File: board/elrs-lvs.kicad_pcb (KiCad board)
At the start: 4 copper layers, 46 x 22 mm, 85 parts, among them J1 PWM, J10 CF/Prog, J12 Balance, J13 U.FL, J2 PWM, J3 PWM, J4 PWM, J5 PWM, J6 PWM, J7 PWM, J8 PWM, J9 Little Tower, SW1 SW_SPST, SW2 SW_SPST, U1 ESP32-PICO-V3, U2 SX1281, U3 TPSM82901SISR, U4 2450FM07D0034T, Y1 52Mhz TCXO

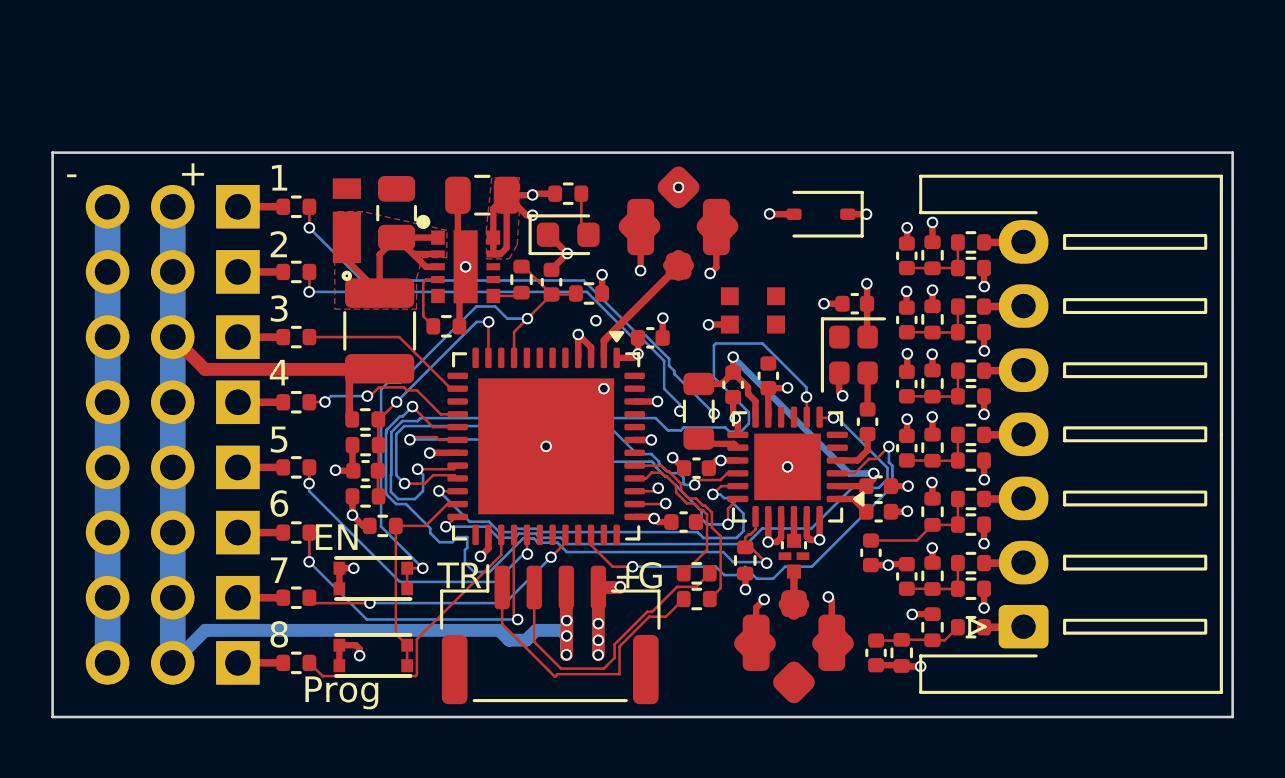
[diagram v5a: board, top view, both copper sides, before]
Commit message: rotate and initial route
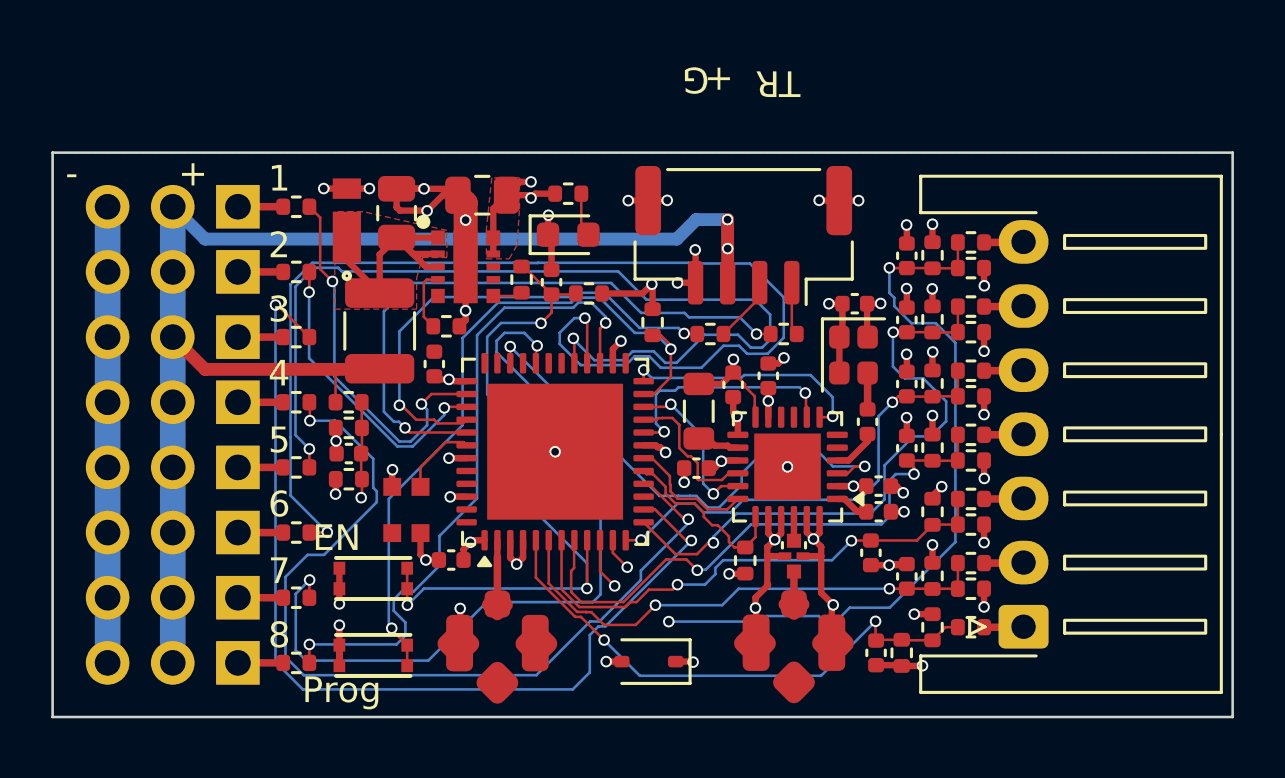
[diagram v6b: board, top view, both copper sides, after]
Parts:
- moved D2 18.7 mm to (23.2, 19.8)
- moved J9 17.7 mm to (17.3, 19.1), turned to -135 degrees
- moved J10 17.3 mm to (26.9, 3.22), turned to 180 degrees
- moved D4 15.6 mm to (13.8, 13.9), turned to -90 degrees
- moved R13 13.2 mm to (23.4, 6.61), turned to -90 degrees
- moved C4 11.6 mm to (15.5, 15.9), turned to 0 degrees
- moved C3 11.5 mm to (14.9, 8.24), turned to -90 degrees
- moved R48 10.9 mm to (28.5, 7.07), turned to 180 degrees
- moved R47 9.35 mm to (25.6, 7.07)
- moved R30 0.93 mm to (11.5, 9.73)
- moved C21 0.93 mm to (11.6, 11.7)
- moved R38 0.93 mm to (11.6, 12.7)
- moved R46 0.93 mm to (11.6, 10.7)
- moved U1 0.41 mm to (19.6, 11.7), turned to 90 degrees
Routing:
- net /PWM6: track 13.6 -> 46.3 mm
- net /PWM3: track 6.61 -> 38.0 mm, vias 0 -> 2
- net /LVS7: track 3.32 -> 33.2 mm, vias 0 -> 3
- net GND: track 211.2 -> 240.5 mm, vias 40 -> 43
- net /PWM4: track 6.45 -> 34.6 mm
- net /PWM5: track 12.1 -> 38.0 mm
- net /RADIO_DIO1: track 30.1 -> 9.42 mm
- net /LVS6: track 3.00 -> 23.7 mm, vias 0 -> 2
- net /PWM7: track 11.4 -> 31.0 mm
- net /RADIO_NSS: track 26.5 -> 6.94 mm, vias 2 -> 0
- net /LVS4: track 3.00 -> 22.5 mm, vias 0 -> 2
- net /BOOT: track 8.39 -> 27.3 mm, vias 0 -> 2
- net /LVS1: track 3.42 -> 21.3 mm, vias 0 -> 2
- net /LVS2: track 3.00 -> 19.9 mm, vias 0 -> 2
- net /SERIAL_TX: track 7.61 -> 23.8 mm, vias 0 -> 2
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
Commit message: cleanup
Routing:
- net +5V: track 53.7 -> 90.5 mm
- net GND: track 240.5 -> 260.9 mm
- net +3.3V: track 121.7 -> 122.3 mm

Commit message: more cleanup
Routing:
- net GND: track 260.9 -> 265.5 mm, vias 43 -> 48
- net /PWM2: track 11.7 -> 12.6 mm
- net /BOOT: track 27.3 -> 27.8 mm
- net /PWM6: track 46.3 -> 46.8 mm
